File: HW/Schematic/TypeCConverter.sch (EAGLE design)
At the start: 41 parts, among them U2 CP2104

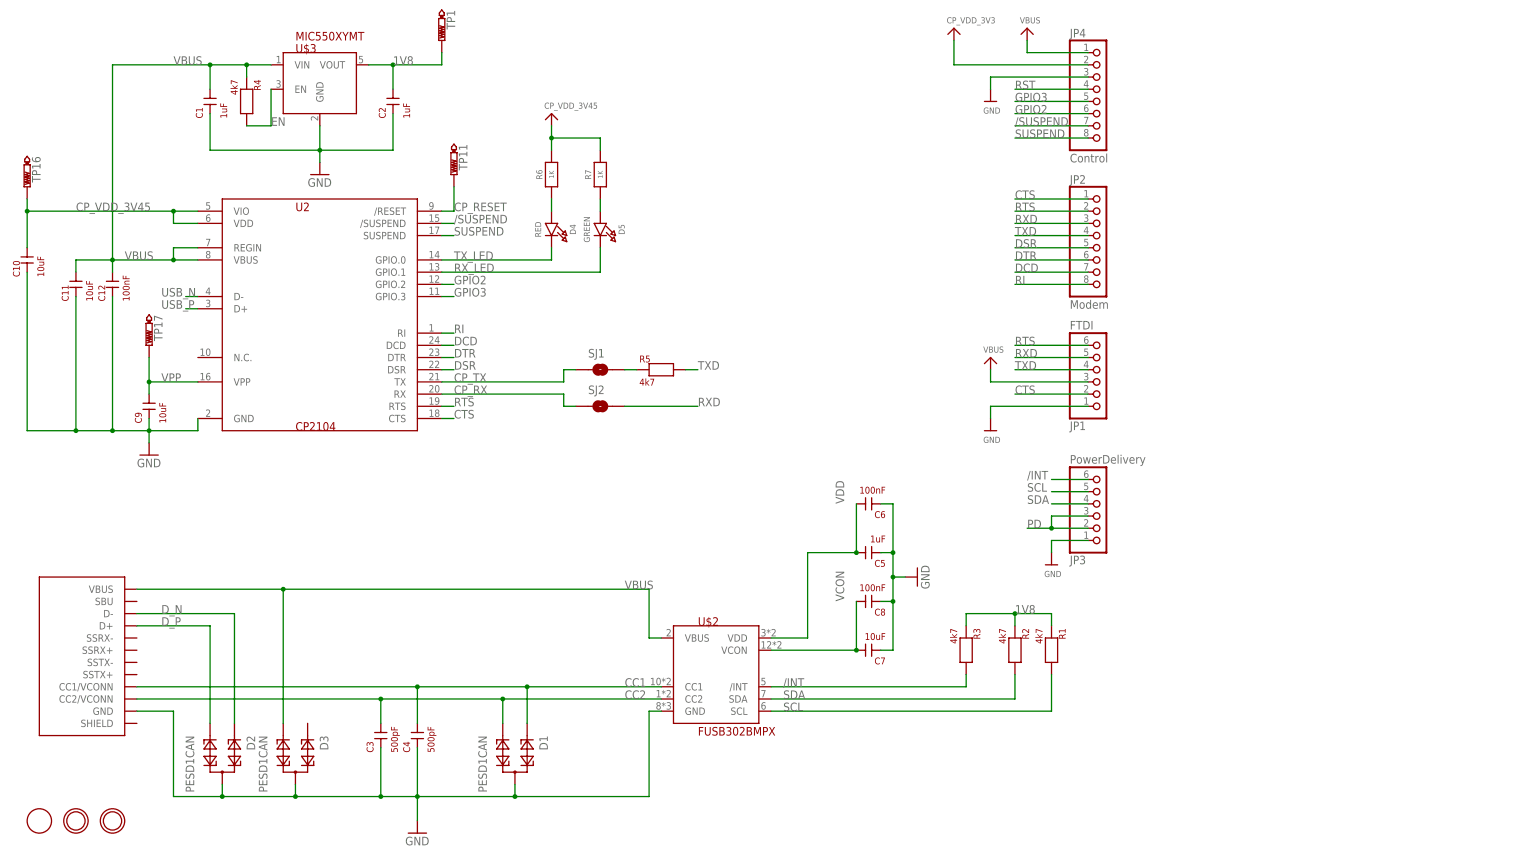
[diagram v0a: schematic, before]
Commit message: Add TPS55165
Add TPS55165 and it’s circuitry
layout file is created
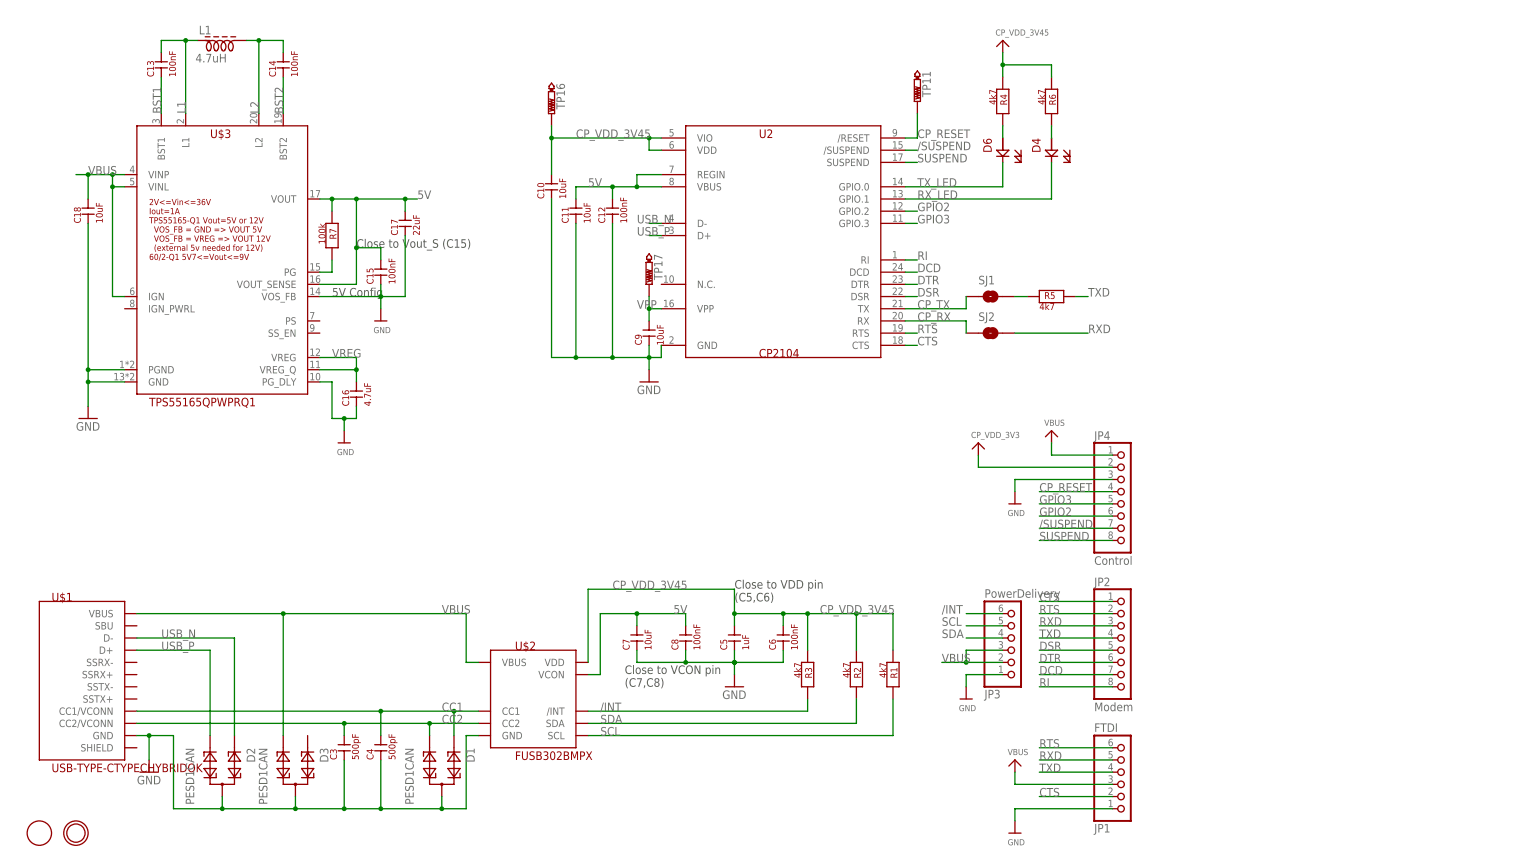
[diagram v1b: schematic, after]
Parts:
- removed C1, C2: 1uF, capacitor:C
- removed D5: GREEN, microbuilder:LED0805_NOOUTLINE
- removed TP1: CP_RESET, testpad:PTR1B1,27
- removed U$18: MOUNTINGHOLE2.0, microbuilder:MOUNTINGHOLE2.0
- added C13, C14, C15: 100nF, capacitor:C
- added C16: 4.7uF, capacitor:C
- added C17: 22uF, capacitor:C
- added C18: 10uF, capacitor:C
- added D6: LED, LED:LED
- added L1: 4.7uH, Inductor:INDUCTOR
- D4: value RED -> LED; device microbuilder:LED0805_NOOUTLINE -> LED:LED
- R6: value 1K -> 4k7; device microbuilder:RESISTOR0805_NOOUTLINE -> resistor:RESISTOR
- R7: value 1K -> 100k; device microbuilder:RESISTOR0805_NOOUTLINE -> resistor:RESISTOR
- U$1: value USB-TYPE-CHYBRID -> USB-TYPE-CTYPECHYBRIDOK; device lio:USB-TYPE-CHYBRID -> lio:USB-TYPE-CTYPECHYBRIDOK
- U$3: value MIC550XYMT -> TPS55165QPWPRQ1; device LDO:MIC550XYMT -> TPS55165QPWPRQ1:TPS55165QPWPRQ1
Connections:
- removed net 1V8: C2.__, R1._, R2._, R3._, TP1.TP, U$3.VOUT
- removed net D_N: D2.1, U$1.D-
- removed net D_P: D2.2, U$1.D+
- removed net EN: R4.__, U$3.EN
- removed net PD: JP3.2, JP3.3
- removed net RST: JP4.4
- removed net VCON: C7.__, C8.__, U$2.VCON
- removed net VDD: C5.__, C6.__, U$2.VDD
- new net 5V: C11.__, C12.__, C15.__, C17.__, C7.__, C8.__, R7._, U$2.VCON, U$3.VOUT, U$3.VOUT_SENSE, U2.REGIN, U2.VBUS
- new net BST1: C13._, U$3.BST1
- new net BST2: C14._, U$3.BST2
- new net L1: C13.__, L1.1, U$3.L1
- new net L2: C14.__, L1.2, U$3.L2
- new net PG: R7.__, U$3.PG
- new net VREG: C16.__, U$3.VREG, U$3.VREG_Q
- net CP_RESET: now also JP4.4
- net CP_VDD_3V45: now also C5.__, C6.__, R1._, R2._, R3._, R4._, R6._, U$2.VDD; no longer R6.2, R7.2
- net GND: now also C15._, C16._, C17._, C18._, U$3.PGND, U$3.PG_DLY, U$3.VOS_FB; no longer C1._, C2._
- net RXLEDWP: now also D4._, R6.__; no longer D5.A, R7.1
- net RX_LED: now also D4.__; no longer D5.C
- net TXLEDWP: now also D6._, R4.__; no longer D4.A, R6.1
- net TX_LED: now also D6.__; no longer D4.C
- net USB_N: now also D2.1, U$1.D-
- net USB_P: now also D2.2, U$1.D+
- net VBUS: now also C18.__, JP3.2, JP3.3, U$3.IGN, U$3.VINL, U$3.VINP; no longer C1.__, C11.__, C12.__, R4._, U$3.VIN, U2.REGIN, U2.VBUS
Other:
- note added: "5V Config"
- note added: "5V Voltage regulator (Buck-Boost)"
- note added: "Close to VCON pin (C7,C8)"
- note added: "Close to VDD pin (C5,C6)"
- note added: "Close to Vout_S (C15)"
- note added: "Power Delivery Interface"
- note added: "USB To UART Converter LDO 3.45V"
- note added: "USB Type C connector ESD Protection"
- moved on the sheet: C10, C11, C12, C3, C4, C5, C6, C7, C8, C9, D1, D2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

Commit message: Finish pre layout
Generate layout pdfs
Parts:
- removed C13, C14, C15: 100nF, capacitor:C
- removed C16: 4.7uF, capacitor:C
- removed C17: 22uF, capacitor:C
- removed C18: 10uF, capacitor:C
- removed L1: 4.7uH, Inductor:INDUCTOR
- removed U$3: TPS55165QPWPRQ1, TPS55165QPWPRQ1:TPS55165QPWPRQ1
- added C34: 2.2uF, capacitor:C1206
- added C35: 0.01uF, capacitor:C
- added C36, C41: 0.1uF, capacitor:C
- added C37: 2.7nF, capacitor:C
- added C38: 6.8pF, capacitor:C
- added C39: 47uF, capacitor:C1206
- added C40: 100nF, capacitor:C
- added D5, D7: LED, LED:LED
- added D8: DIODESMB, Diode:DIODESMB
- added L4: 10uH, Inductor:INDUCTOR
- added R16: 90.9k, resistor:RESISTOR
- added R17, R18: (no value), resistor:RESISTOR
- added R19: 76.8k, resistor:RESISTOR
- added R8: 4k7, resistor:RESISTOR
- added TP1, TP10, TP12, TP3, TP4, TP5, TP6, TP7, TP8, TP9: CP_RESET, testpad:PTR1B1,27
- added U$11: TPS57140QDRCRQ1, PMIC:TPS57140QDRCRQ1
- R7: value 100k -> 4k7
- U$1: value USB-TYPE-CTYPECHYBRIDOK -> USB-TYPE-CTYPEC_SMT; device lio:USB-TYPE-CTYPECHYBRIDOK -> lio:USB-TYPE-CTYPEC_SMT
- renumbered U$19 to GND
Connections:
- removed net BST1: C13._, U$3.BST1
- removed net BST2: C14._, U$3.BST2
- removed net L2: C14.__, L1.2, U$3.L2
- removed net PG: R7.__, U$3.PG
- removed net VREG: C16.__, U$3.VREG, U$3.VREG_Q
- new net 3V45LEDWP: D7._, R8.__, TP12.TP
- new net 5VLEDWP: D5._, R7.__, TP10.TP
- new net BOOT: C36._, U$11.BOOT
- new net CLK: R16.__, TP3.TP, U$11.RT/CLK
- new net COMP: C38._, R19.__, TP9.TP, U$11.COMP
- new net COMP_S: C37.__, R19._
- new net EN: U$11.EN
- new net PGOOD: TP11.TP, U$11.PGOOD
- new net SS/TR: C35.__, TP1.TP, U$11.SS/TR
- new net VSNS: R17._, R18.__, TP4.TP, U$11.VSNS
- net 5V: now also C39.__, C40.__, JP1.3, JP4.1, L4.2, R18._; no longer C15.__, C17.__, U$3.VOUT, U$3.VOUT_SENSE
- net CC1: now also TP7.TP
- net CC2: now also TP8.TP
- net CP_RESET: no longer TP11.TP
- net CP_VDD_3V45: now also R8._
- net GND: now also C34._, C35._, C37._, C38.__, C39._, C40._, C41._, D5.__, D7.__, D8.A, R16._, R17.__, U$11.GND; no longer C15._, C16._, C17._, C18._, U$3.GND, U$3.PGND, U$3.PG_DLY, U$3.VOS_FB
- net L1: now also C36.__, D8.C, L4.1, U$11.PH; no longer C13.__, L1.1, U$3.L1
- net RXLEDWP: now also TP6.TP
- net TXLEDWP: now also TP5.TP
- net VBUS: now also C34.__, C41.__, U$11.VIN; no longer C18.__, JP1.3, JP4.1, U$3.IGN, U$3.VINL, U$3.VINP
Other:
- note removed: "5V Config"
- note removed: "5V Voltage regulator (Buck-Boost)"
- note removed: "Close to Vout_S (C15)"
- moved on the sheet: C10, C11, C12, C9, D4, D6, R4, R5, R6, R7, SJ1, SJ2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

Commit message: Add BOM
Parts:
- removed C9: 10uF, capacitor:C
- removed TP17: VPP, testpad:PTR1B1,27
- R17: value (none) -> 10k 1%
- R18: value (none) -> 52.5k 1%
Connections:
- removed net VPP: C9.__, TP17.TP, U2.VPP
- net GND: no longer C9._
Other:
- note added: "R18 = R17 * ((Vout-0.8V)/0.8) R17 = 10k and both resistors are 1%"
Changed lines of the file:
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@@
 <part name="GND3" library="SparkFun-Aesthetics" deviceset="GND" device=""/>
 <part name="U2" library="CP2104" deviceset="CP2104" device="" package3d_urn="urn:adsk.eagle:package:2401500/1"/>
-<part name="C9" library="capacitor" deviceset="C" device="" package3d_urn="urn:adsk.eagle:package:23679/2" value="10uF"/>
 <part name="R5" library="resistor" deviceset="RESISTOR" device="" package3d_urn="urn:adsk.eagle:package:970935/2" value="4k7"/>
 <part name="C10" library="capacitor" deviceset="C" device="" package3d_urn="urn:adsk.eagle:package:23679/2" value="10uF"/>
@@
 <part name="SJ2" library="SparkFun-Retired" deviceset="SOLDERJUMPER-OLD" device="TRACE" value=""/>
 <part name="SJ1" library="SparkFun-Retired" deviceset="SOLDERJUMPER-OLD" device="TRACE" value=""/>
-<part name="TP17" library="testpad" deviceset="PTR1" device="B1,27" value="VPP"/>
 <part name="TP16" library="testpad" deviceset="PTR1" device="B1,27" value="CP_RESET"/>
 <part name="D1" library="diode" library_urn="urn:adsk.eagle:library:210" deviceset="PESD1CAN" device="" package3d_urn="urn:adsk.eagle:package:43389/2"/>
@@
 <part name="C36" library="capacitor" deviceset="C" device="" package3d_urn="urn:adsk.eagle:package:23679/2" value="0.1uF"/>
 <part name="L4" library="Inductor" deviceset="INDUCTOR" device="" package3d_urn="urn:adsk.eagle:package:6883134/1" value="10uH"/>
-<part name="R17" library="resistor" deviceset="RESISTOR" device="" package3d_urn="urn:adsk.eagle:package:970935/2"/>
-<part name="R18" library="resistor" deviceset="RESISTOR" device="" package3d_urn="urn:adsk.eagle:package:970935/2"/>
+<part name="R17" library="resistor" deviceset="RESISTOR" device="" package3d_urn="urn:adsk.eagle:package:970935/2" value="10k 1%"/>
+<part name="R18" library="resistor" deviceset="RESISTOR" device="" package3d_urn="urn:adsk.eagle:package:970935/2" value="52.5k 1%"/>
 <part name="C37" library="capacitor" deviceset="C" device="" package3d_urn="urn:adsk.eagle:package:23679/2" value="2.7nF"/>
 <part name="C38" library="capacitor" deviceset="C" device="" package3d_urn="urn:adsk.eagle:package:23679/2" value="6.8pF"/>
@@
 <text x="30.48" y="73.66" size="2.54" layer="150" font="vector">USB Type C connector
 ESD Protection</text>
+<text x="116.84" y="119.38" size="1.778" layer="97">R18 = R17 * ((Vout-0.8V)/0.8)
+R17 = 10k and both resistors are 1%</text>
 </plain>
 <instances>
@@
 <instance part="GND3" gate="1" x="157.48" y="38.1"/>
 <instance part="U2" gate="G$1" x="251.46" y="129.54"/>
-<instance part="C9" gate="G$1" x="226.06" y="109.22" rot="R90"/>
 <instance part="R5" gate="G$1" x="309.88" y="116.84"/>
 <instance part="C10" gate="G$1" x="205.74" y="139.7" rot="R90"/>
@@
 <instance part="SJ2" gate="1" x="297.18" y="109.22"/>
 <instance part="SJ1" gate="1" x="297.18" y="116.84"/>
-<instance part="TP17" gate="G$1" x="226.06" y="119.38" rot="R180"/>
 <instance part="TP16" gate="G$1" x="205.74" y="154.94" rot="R180"/>
 <instance part="D1" gate="G$1" x="96.52" y="20.32" rot="R270"/>
@@
 <wire x1="226.06" y1="104.14" x2="228.6" y2="104.14" width="0.1524" layer="91"/>
 <wire x1="228.6" y1="104.14" x2="228.6" y2="106.68" width="0.1524" layer="91"/>
-<pinref part="C9" gate="G$1" pin="_"/>
-<wire x1="226.06" y1="106.68" x2="226.06" y2="104.14" width="0.1524" layer="91"/>
 <junction x="226.06" y="104.14"/>
 <junction x="218.44" y="104.14"/>
@@
 </segment>
 </net>
-<net name="VPP" class="0">
-<segment>
-<pinref part="U2" gate="G$1" pin="VPP"/>
-<pinref part="C9" gate="G$1" pin="__"/>
-<wire x1="228.6" y1="114.3" x2="226.06" y2="114.3" width="0.1524" layer="91"/>
-<label x="223.52" y="114.3" size="1.778" layer="95"/>
-<pinref part="TP17" gate="G$1" pin="TP"/>
-<wire x1="226.06" y1="114.3" x2="226.06" y2="111.76" width="0.1524" layer="91"/>
-<wire x1="226.06" y1="116.84" x2="226.06" y2="114.3" width="0.1524" layer="91"/>
-<junction x="226.06" y="114.3"/>
-</segment>
-</net>
